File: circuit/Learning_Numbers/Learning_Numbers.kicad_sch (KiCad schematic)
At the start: 106 parts, among them SW1 SW_DIP_x01, SW10 SW_Push, SW11 SW_Push, SW12 SW_Push, SW13 SW_Push, SW14 SW_Push, SW15 SW_Push, SW16 SW_Push, SW17 SW_Push, SW18 SW_Push, SW19 SW_Push, SW2 SW_Push, SW20 SW_Push, SW21 SW_Push, SW22 SW_Push, SW23 SW_Push, SW3 SW_Push, SW4 SW_Push, SW5 SW_Push, SW6 SW_Push, SW7 SW_Push, SW8 SW_Push, SW9 SW_Push, U1 ATmega168PA-P, U2 74HC165, U3 74HC165, U4 74HC595, U5 74HC595, U6 74HC595, U7 74HC595, U8 74HC595

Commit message: finish circuit pathing
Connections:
- net LATCH: now also U4.12 (RCLK)
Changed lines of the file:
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@@
+	(wire
+		(pts
+			(xy 95.25 40.64) (xy 97.79 40.64)
+		)
+		(stroke
+			(width 0)
+			(type default)
+		)
+	)
 	(wire
 		(pts

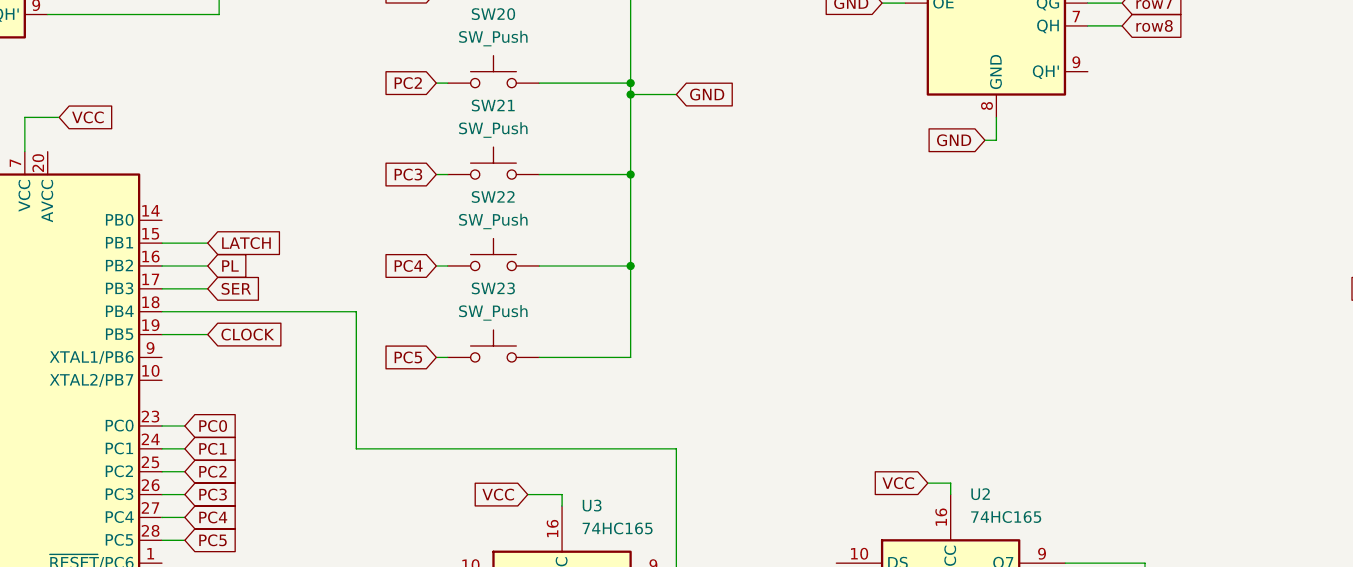
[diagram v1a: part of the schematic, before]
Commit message: add crystal to circuit
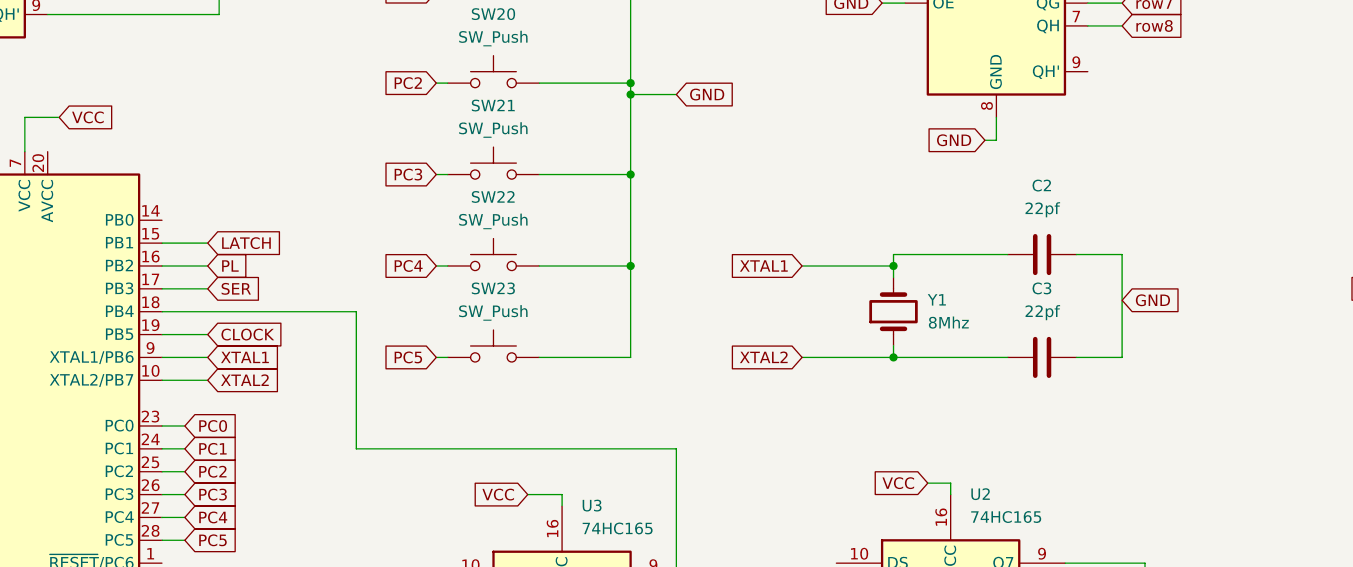
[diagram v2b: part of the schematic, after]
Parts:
- added C2, C3: 22pf, Capacitor_SMD:C_1206_3216Metric_Pad1.33x1.80mm_HandSolder, symbol Device:C
- added Y1: 8Mhz, Crystal:Crystal_HC49-4H_Vertical, symbol Device:Crystal
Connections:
- net GND: now also C2.2, C3.2
- net XTAL2: now reaches U1.10 (XTAL2/PB7)
- net XTAL2: now also C3.1, Y1.1
- net XTAL1: now reaches U1.9 (XTAL1/PB6)
- net XTAL1: now also C2.1, Y1.2

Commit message: update pcb silk layer
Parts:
- SW1: value SW_DIP_x01 -> Power Switch
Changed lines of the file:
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@@
 			)
 		)
-		(property "Value" "SW_DIP_x01"
+		(property "Value" "Power Switch"
 			(at 57.15 219.71 0)
 			(effects

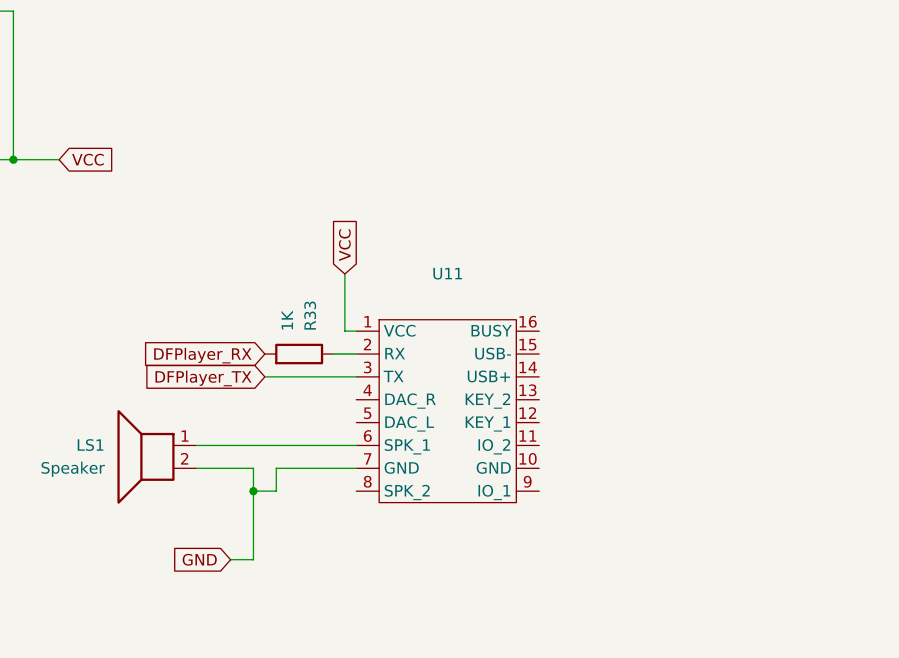
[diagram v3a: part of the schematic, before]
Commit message: update circuit add capacitor DFPlayer and change speaker conections
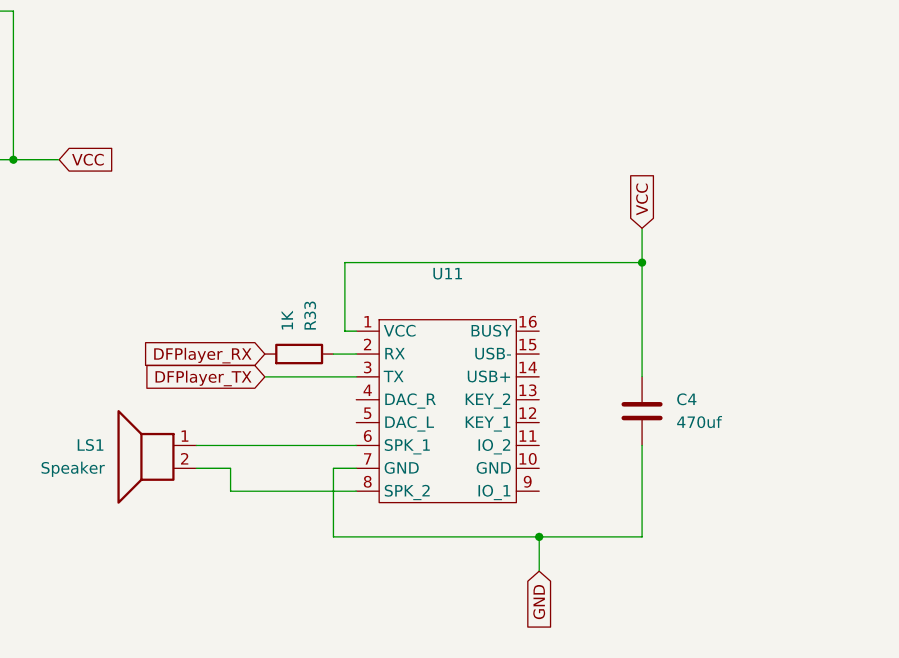
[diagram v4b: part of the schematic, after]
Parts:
- added C4: 470uf, Capacitor_SMD:C_Elec_8x10.2, symbol Device:C
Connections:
- net GND: now also C4.2; no longer LS1.2
- net VCC: now also C4.1
- net at U11.8 (SPK_2): now also LS1.2
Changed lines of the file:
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@@
 	)
 	(junction
+		(at 127 266.7)
+		(diameter 0)
+		(color 0 0 0 0)
+	)
+	(junction
+		(at 138.43 236.22)
+		(diameter 0)
+		(color 0 0 0 0)
+	)
+	(junction
 		(at 297.18 121.92)
 		(diameter 0)
@@
 	)
 	(junction
-		(at 95.25 261.62)
-		(diameter 0)
-		(color 0 0 0 0)
-	)
-	(junction
 		(at 335.28 121.92)
 		(diameter 0)
@@
 	(wire
 		(pts
-			(xy 237.49 224.79) (xy 236.22 224.79)
+			(xy 127 270.51) (xy 127 266.7)
 		)
 		(stroke
@@
 	(wire
 		(pts
-			(xy 128.27 27.94) (xy 139.7 27.94)
+			(xy 237.49 224.79) (xy 236.22 224.79)
 		)
 		(stroke
@@
 	(wire
 		(pts
-			(xy 109.22 88.9) (xy 109.22 99.06)
+			(xy 128.27 27.94) (xy 139.7 27.94)
 		)
 		(stroke
@@
 	(wire
 		(pts
-			(xy 118.11 45.72) (xy 120.65 45.72)
+			(xy 109.22 88.9) (xy 109.22 99.06)
 		)
 		(stroke
@@
 	(wire
 		(pts
-			(xy 130.81 160.02) (xy 132.08 160.02)
+			(xy 118.11 45.72) (xy 120.65 45.72)
 		)
 		(stroke
@@
 	(wire
 		(pts
-			(xy 92.71 269.24) (xy 95.25 269.24)
+			(xy 130.81 160.02) (xy 132.08 160.02)
 		)
 		(stroke
@@
 	(wire
 		(pts
-			(xy 95.25 269.24) (xy 95.25 261.62)
+			(xy 92.71 259.08) (xy 92.71 261.62)
 		)
 		(stroke
@@
 	(wire
 		(pts
+			(xy 138.43 236.22) (xy 105.41 236.22)
+		)
+		(stroke
+			(width 0)
+			(type default)
+		)
+	)
+	(wire
+		(pts
 			(xy 44.45 81.28) (xy 48.26 81.28)
 		)
@@
 	(wire
 		(pts
+			(xy 92.71 261.62) (xy 106.68 261.62)
+		)
+		(stroke
+			(width 0)
+			(type default)
+		)
+	)
+	(wire
+		(pts
 			(xy 203.2 212.09) (xy 204.47 212.09)
 		)
@@
 	(wire
 		(pts
+			(xy 138.43 232.41) (xy 138.43 236.22)
+		)
+		(stroke
+			(width 0)
+			(type default)
+		)
+	)
+	(wire
+		(pts
 			(xy 204.47 234.95) (xy 204.47 238.76)
 		)
@@
 	(wire
 		(pts
+			(xy 104.14 259.08) (xy 106.68 259.08)
+		)
+		(stroke
+			(width 0)
+			(type default)
+		)
+	)
+	(wire
+		(pts
 			(xy 247.65 203.2) (xy 267.97 203.2)
 		)
@@
 	(wire
 		(pts
-			(xy 105.41 237.49) (xy 105.41 243.84)
-		)
-		(stroke
-			(width 0)
-			(type default)
-		)
-	)
-	(wire
-		(pts
 			(xy 130.81 154.94) (xy 132.08 154.94)
 		)
@@
 	(wire
 		(pts
+			(xy 105.41 236.22) (xy 105.41 243.84)
+		)
+		(stroke
+			(width 0)
+			(type default)
+		)
+	)
+	(wire
+		(pts
 			(xy 45.72 102.87) (xy 41.91 102.87)
 		)
@@
 	(wire
 		(pts
-			(xy 97.79 261.62) (xy 95.25 261.62)
-		)
-		(stroke
-			(width 0)
-			(type default)
-		)
-	)
-	(wire
-		(pts
 			(xy 118.11 40.64) (xy 120.65 40.64)
 		)
@@
 	(wire
 		(pts
-			(xy 130.81 157.48) (xy 132.08 157.48)
+			(xy 127 266.7) (xy 104.14 266.7)
 		)
 		(stroke
@@
 	(wire
 		(pts
-			(xy 328.93 210.82) (xy 328.93 222.25)
+			(xy 130.81 157.48) (xy 132.08 157.48)
 		)
 		(stroke
@@
 	(wire
 		(pts
-			(xy 34.29 55.88) (xy 34.29 54.61)
+			(xy 328.93 210.82) (xy 328.93 222.25)
 		)
 		(stroke
@@
 	(wire
 		(pts
-			(xy 248.92 104.14) (xy 248.92 113.03)
+			(xy 34.29 55.88) (xy 34.29 54.61)
 		)
 		(stroke
@@
 	(wire
 		(pts
-			(xy 95.25 259.08) (xy 88.9 259.08)
+			(xy 248.92 104.14) (xy 248.92 113.03)
 		)
 		(stroke
@@
 	(wire
 		(pts
+			(xy 138.43 236.22) (xy 138.43 248.92)
+		)
+		(stroke
+			(width 0)
+			(type default)
+		)
+	)
+	(wire
+		(pts
 			(xy 246.38 210.82) (xy 248.92 210.82)
 		)
@@
 	(wire
 		(pts
+			(xy 104.14 266.7) (xy 104.14 259.08)
+		)
+		(stroke
+			(width 0)
+			(type default)
+		)
+	)
+	(wire
+		(pts
 			(xy 223.52 210.82) (xy 226.06 210.82)
 		)
@@
 	(wire
 		(pts
+			(xy 127 266.7) (xy 138.43 266.7)
+		)
+		(stroke
+			(width 0)
+			(type default)
+		)
+	)
+	(wire
+		(pts
 			(xy 130.81 167.64) (xy 132.08 167.64)
 		)
@@
 	(wire
 		(pts
-			(xy 118.11 33.02) (xy 120.65 33.02)
+			(xy 88.9 259.08) (xy 92.71 259.08)
 		)
 		(stroke
@@
 	(wire
 		(pts
-			(xy 99.06 196.85) (xy 101.6 196.85)
+			(xy 118.11 33.02) (xy 120.65 33.02)
 		)
 		(stroke
@@
 	(wire
 		(pts
-			(xy 328.93 222.25) (xy 328.93 227.33)
+			(xy 99.06 196.85) (xy 101.6 196.85)
 		)
 		(stroke
@@
 	(wire
 		(pts
-			(xy 97.79 259.08) (xy 97.79 261.62)
+			(xy 328.93 222.25) (xy 328.93 227.33)
 		)
 		(stroke
@@
 	(wire
 		(pts
+			(xy 138.43 266.7) (xy 138.43 256.54)
+		)
+		(stroke
+			(width 0)
+			(type default)
+		)
+	)
+	(wire
+		(pts
 			(xy 241.3 45.72) (xy 243.84 45.72)
 		)
@@
 	(wire
 		(pts
-			(xy 106.68 259.08) (xy 97.79 259.08)
-		)
-		(stroke
-			(width 0)
-			(type default)
-		)
-	)
-	(wire
-		(pts
 			(xy 44.45 41.91) (xy 48.26 41.91)
 		)
@@
 	(wire
 		(pts
-			(xy 95.25 261.62) (xy 95.25 259.08)
-		)
-		(stroke
-			(width 0)
-			(type default)
-		)
-	)
-	(wire
-		(pts
 			(xy 38.1 191.77) (xy 41.91 191.77)
 		)
@@
 	(global_label "VCC"
 		(shape input)
-		(at 105.41 237.49 90)
+		(at 138.43 232.41 90)
 		(fields_autoplaced yes)
 		(effects
@@
 		)
 		(property "Intersheetrefs" "${INTERSHEET_REFS}"
-			(at 105.41 230.8762 90)
+			(at 138.43 225.7962 90)
 			(effects
 				(font
@@
 	(global_label "GND"
 		(shape input)
-		(at 92.71 269.24 180)
+		(at 127 270.51 270)
 		(fields_autoplaced yes)
 		(effects
@@
 		)
 		(property "Intersheetrefs" "${INTERSHEET_REFS}"
-			(at 85.8543 269.24 0)
+			(at 127 277.3657 90)
 			(effects
 				(font
@@
 					(unit 1)
 				)
+			)
+		)
+	)
+	(symbol
+		(lib_id "Device:C")
+		(at 138.43 252.73 0)
+		(unit 1)
+		(exclude_from_sim no)
+		(in_bom yes)
+		(on_board yes)
+		(dnp no)
+		(fields_autoplaced yes)
+		(property "Reference" "C4"
+			(at 142.24 251.4599 0)
+			(effects
+				(font
+					(size 1.27 1.27)
+				)
+				(justify left)
+			)
+		)
+		(property "Value" "470uf"
+			(at 142.24 253.9999 0)
+			(effects
+				(font
+					(size 1.27 1.27)
+				)
+				(justify left)
+			)
+		)
+		(property "Footprint" "Capacitor_SMD:C_Elec_8x10.2"
+			(at 139.3952 256.54 0)
+			(effects
+				(font
+					(size 1.27 1.27)
+				)
+				(hide yes)
+			)
+		)
+		(property "Datasheet" "~"
+			(at 138.43 252.73 0)
+			(effects
+				(font
+					(size 1.27 1.27)
+				)
+				(hide yes)
+			)
+		)
+		(property "Description" "Unpolarized capacitor"
+			(at 138.43 252.73 0)
+			(effects
+				(font
+					(size 1.27 1.27)
+				)
+				(hide yes)
+			)
+		)
+		(pin "1"
+		)
+		(pin "2"
+		)
+		(instances
+			(project ""
+				(path "/890147ce-34b3-4c01-8385-09be83bd6fae"
+					(reference "C4")
+					(unit 1)
+				)

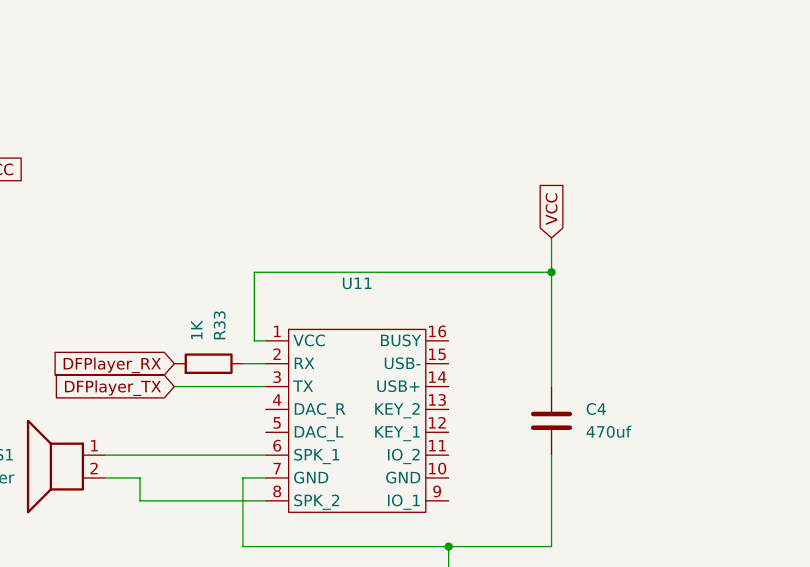
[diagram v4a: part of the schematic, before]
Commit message: Update circuit to add DFPlayer 10 ohm resistor
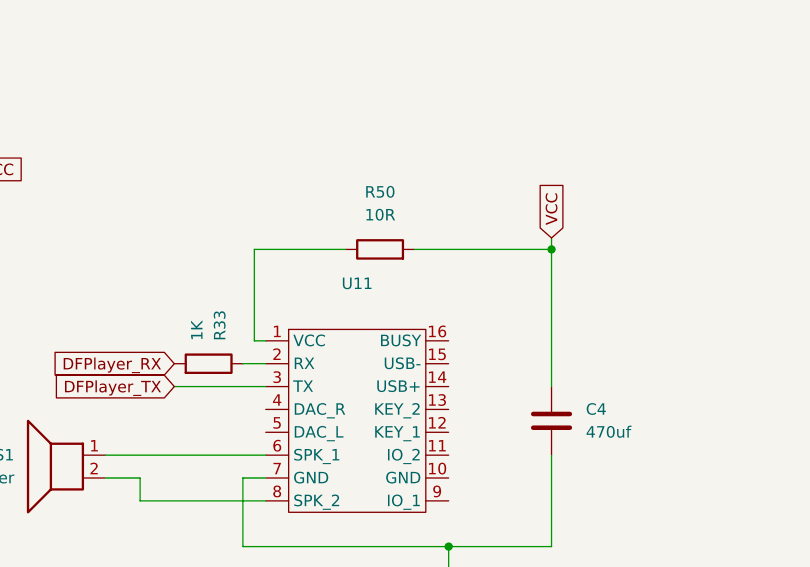
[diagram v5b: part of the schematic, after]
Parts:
- added R50: 10R, Resistor_SMD:R_1206_3216Metric_Pad1.30x1.75mm_HandSolder, symbol Device:R
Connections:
- net VCC: now also R50.2; no longer U11.1 (VCC)
- new net: R50.1, U11.1 (VCC)
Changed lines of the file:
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@@
 	)
 	(junction
+		(at 138.43 233.68)
+		(diameter 0)
+		(color 0 0 0 0)
+	)
+	(junction
 		(at 328.93 238.76)
 		(diameter 0)
@@
 	)
 	(junction
-		(at 138.43 236.22)
-		(diameter 0)
-		(color 0 0 0 0)
-	)
-	(junction
 		(at 297.18 121.92)
 		(diameter 0)
@@
 	(wire
 		(pts
-			(xy 138.43 236.22) (xy 105.41 236.22)
-		)
-		(stroke
-			(width 0)
-			(type default)
-		)
-	)
-	(wire
-		(pts
 			(xy 44.45 81.28) (xy 48.26 81.28)
 		)
@@
 	(wire
 		(pts
-			(xy 138.43 232.41) (xy 138.43 236.22)
-		)
-		(stroke
-			(width 0)
-			(type default)
-		)
-	)
-	(wire
-		(pts
 			(xy 204.47 234.95) (xy 204.47 238.76)
 		)
@@
 	(wire
 		(pts
+			(xy 123.19 233.68) (xy 138.43 233.68)
+		)
+		(stroke
+			(width 0)
+			(type default)
+		)
+	)
+	(wire
+		(pts
 			(xy 346.71 199.39) (xy 346.71 203.2)
 		)
@@
 	(wire
 		(pts
-			(xy 105.41 236.22) (xy 105.41 243.84)
+			(xy 105.41 233.68) (xy 105.41 243.84)
 		)
 		(stroke
@@
 	(wire
 		(pts
-			(xy 138.43 236.22) (xy 138.43 248.92)
+			(xy 138.43 232.41) (xy 138.43 233.68)
 		)
 		(stroke
@@
 	(wire
 		(pts
+			(xy 138.43 233.68) (xy 138.43 248.92)
+		)
+		(stroke
+			(width 0)
+			(type default)
+		)
+	)
+	(wire
+		(pts
 			(xy 107.95 58.42) (xy 107.95 55.88)
 		)
@@
 	(wire
 		(pts
+			(xy 105.41 233.68) (xy 115.57 233.68)
+		)
+		(stroke
+			(width 0)
+			(type default)
+		)
+	)
+	(wire
+		(pts
 			(xy 222.25 138.43) (xy 215.9 138.43)
 		)
@@
 					(unit 1)
 				)
+			)
+		)
+	)
+	(symbol
+		(lib_id "Device:R")
+		(at 119.38 233.68 90)
+		(unit 1)
+		(exclude_from_sim no)
+		(in_bom yes)
+		(on_board yes)
+		(dnp no)
+		(fields_autoplaced yes)
+		(property "Reference" "R50"
+			(at 119.38 227.33 90)
+			(effects
+				(font
+					(size 1.27 1.27)
+				)
+			)
+		)
+		(property "Value" "10R"
+			(at 119.38 229.87 90)
+			(effects
+				(font
+					(size 1.27 1.27)
+				)
+			)
+		)
+		(property "Footprint" "Resistor_SMD:R_1206_3216Metric_Pad1.30x1.75mm_HandSolder"
+			(at 119.38 235.458 90)
+			(effects
+				(font
+					(size 1.27 1.27)
+				)
+				(hide yes)
+			)
+		)
+		(property "Datasheet" "~"
+			(at 119.38 233.68 0)
+			(effects
+				(font
+					(size 1.27 1.27)
+				)
+				(hide yes)
+			)
+		)
+		(property "Description" "Resistor"
+			(at 119.38 233.68 0)
+			(effects
+				(font
+					(size 1.27 1.27)
+				)
+				(hide yes)
+			)
+		)
+		(pin "1"
+		)
+		(pin "2"
+		)
+		(instances
+			(project ""
+				(path "/890147ce-34b3-4c01-8385-09be83bd6fae"
+					(reference "R50")
+					(unit 1)
+				)
